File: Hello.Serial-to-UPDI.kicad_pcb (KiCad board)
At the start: 2 copper layers, 19.7 x 19 mm, 3 parts, among them J1 Conn_01x03_Male, J2 Conn_FTDI_01x06_Male

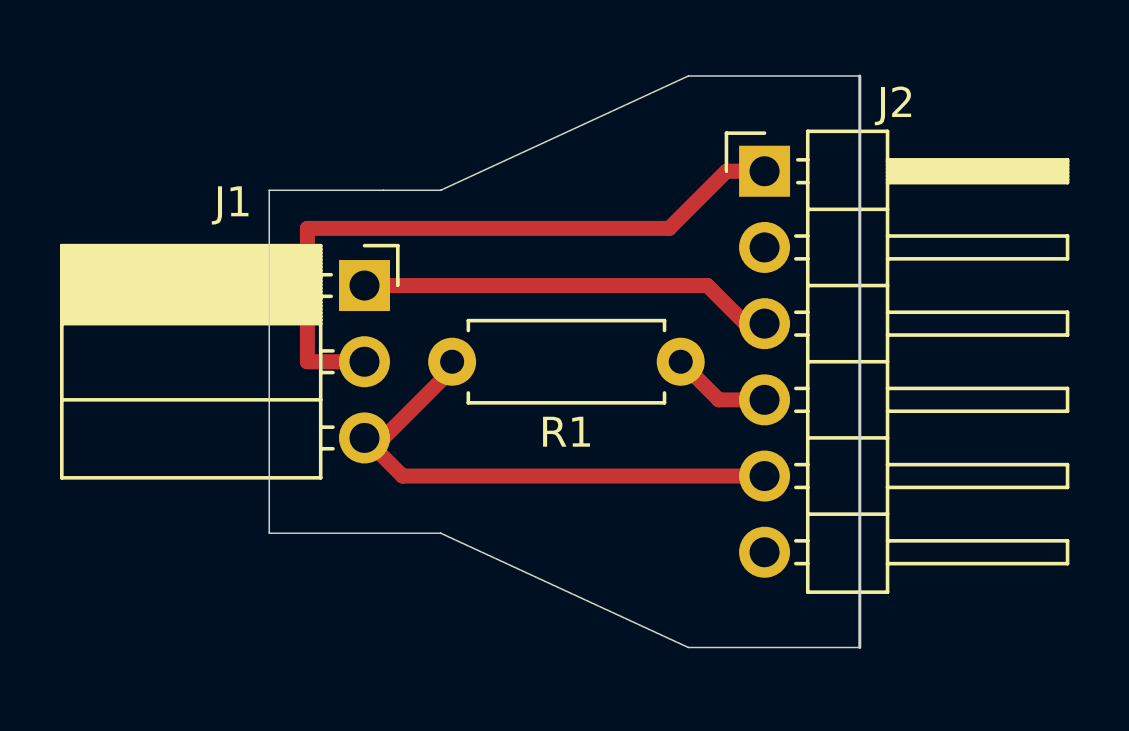
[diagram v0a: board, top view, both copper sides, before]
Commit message: Commit recent RML files, get rid of old SVGs
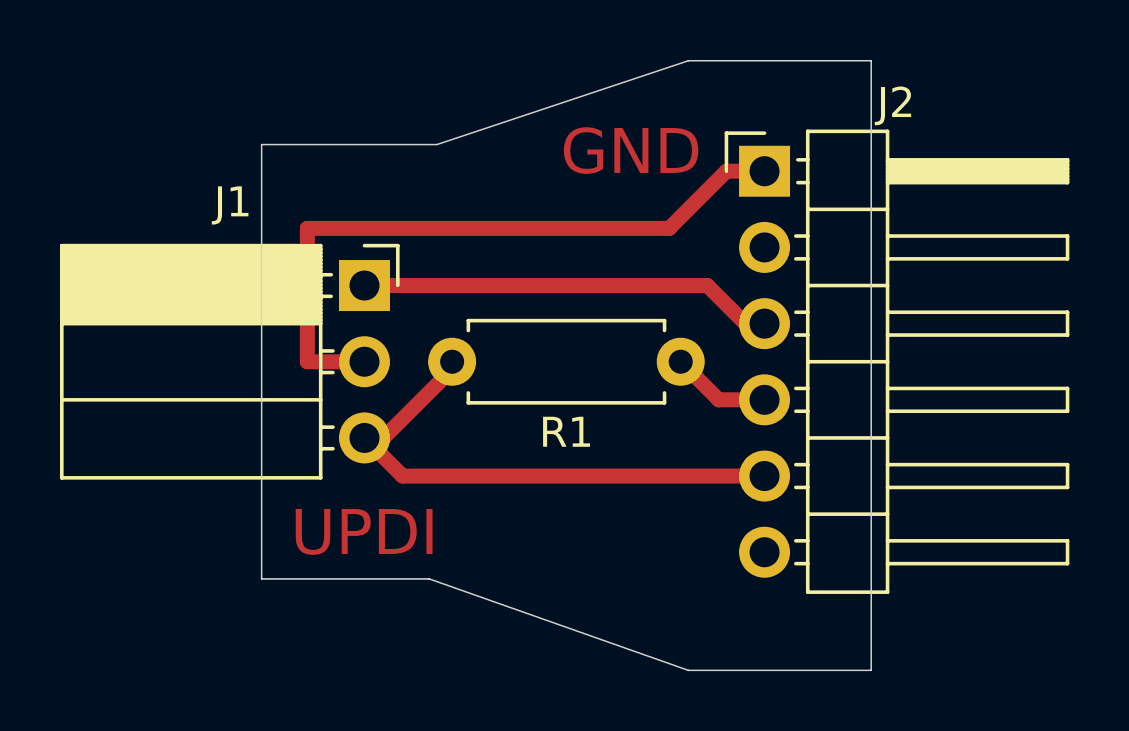
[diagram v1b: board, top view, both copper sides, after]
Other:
- board size 19.7 x 19 mm -> 20.3 x 20.3 mm
- board text added: "GND"
- board text added: "UPDI"
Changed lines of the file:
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@@
-(kicad_pcb (version 20171130) (host pcbnew "(5.1.9)-1")
+(kicad_pcb (version 20171130) (host pcbnew "(5.1.9-0-10_14)")
   (general
     (thickness 1.6)
@@
     (38 B.Mask user)
     (39 F.Mask user)
-    (40 Dwgs.User user hide)
+    (40 Dwgs.User user)
     (41 Cmts.User user)
     (42 Eco1.User user)
     (43 Eco2.User user)
     (44 Edge.Cuts user)
-    (45 Margin user hide)
+    (45 Margin user)
     (46 B.CrtYd user)
     (47 F.CrtYd user)
@@
   )
   (setup
-    (last_trace_width 0.5)
+    (last_trace_width 0.25)
     (user_trace_width 0.5)
     (trace_clearance 0.2)
@@
     (visible_elements 7FFFFFFF)
     (pcbplotparams
-      (layerselection 0x010fc_ffffffff)
+      (layerselection 0x00000_7fffffff)
       (usegerberextensions false)
       (usegerberattributes true)
@@
       (psnegative false)
       (psa4output false)
-      (plotreference true)
-      (plotvalue true)
+      (plotreference false)
+      (plotvalue false)
       (plotinvisibletext false)
-      (padsonsilk false)
+      (padsonsilk true)
       (subtractmaskfromsilk false)
-      (outputformat 1)
+      (outputformat 5)
       (mirror false)
-      (drillshape 1)
+      (drillshape 0)
       (scaleselection 1)
       (outputdirectory ""))
@@
       (effects (font (size 1 1) (thickness 0.15)))
     )
-    (fp_text user %R (at 3.81 0) (layer F.Fab)
-      (effects (font (size 1 1) (thickness 0.15)))
-    )
     (fp_line (start 0.66 -1.25) (end 0.66 1.25) (layer F.Fab) (width 0.1))
     (fp_line (start 0.66 1.25) (end 6.96 1.25) (layer F.Fab) (width 0.1))
@@
     (fp_line (start 8.67 1.5) (end 8.67 -1.5) (layer F.CrtYd) (width 0.05))
     (fp_line (start 8.67 -1.5) (end -1.05 -1.5) (layer F.CrtYd) (width 0.05))
+    (fp_text user %R (at 3.81 0) (layer F.Fab)
+      (effects (font (size 1 1) (thickness 0.15)))
+    )
     (pad 2 thru_hole oval (at 7.62 0 180) (size 1.6 1.6) (drill 0.8) (layers *.Cu *.Mask)
       (net 1 "Net-(J1-Pad3)"))
@@
     )
     (fp_text value Conn_FTDI_01x06_Male (at 4.385 14.97) (layer F.Fab)
-      (effects (font (size 1 1) (thickness 0.15)))
-    )
-    (fp_text user %R (at 2.77 6.35 90) (layer F.Fab)
       (effects (font (size 1 1) (thickness 0.15)))
     )
@@
     (fp_line (start 10.55 14.5) (end 10.55 -1.8) (layer F.CrtYd) (width 0.05))
     (fp_line (start 10.55 -1.8) (end -1.8 -1.8) (layer F.CrtYd) (width 0.05))
+    (fp_text user %R (at 2.77 6.35 90) (layer F.Fab)
+      (effects (font (size 1 1) (thickness 0.15)))
+    )
     (pad 6 thru_hole oval (at 0 12.7) (size 1.7 1.7) (drill 1) (layers *.Cu *.Mask)
       (net 4 "Net-(J2-Pad6)"))
@@
     )
   )
-  (module Connector_PinSocket_2.54mm:PinSocket_1x03_P2.54mm_Horizontal (layer F.Cu)
+  (module Connector_PinSocket_2.54mm:PinSocket_1x03_P2.54mm_Horizontal locked (layer F.Cu)
     (at 135.255 84.455)
     (descr "Through hole angled socket strip, 1x03, 2.54mm pitch, 8.51mm socket length, single row (from Kicad 4.0.7), script generated")
@@
     )
     (fp_text value Conn_01x03_Male (at -4.38 7.85) (layer F.Fab)
-      (effects (font (size 1 1) (thickness 0.15)))
-    )
-    (fp_text user %R (at -5.775 2.54) (layer F.Fab)
       (effects (font (size 1 1) (thickness 0.15)))
     )
@@
     (fp_line (start -10.55 6.85) (end 1.75 6.85) (layer F.CrtYd) (width 0.05))
     (fp_line (start 1.75 6.85) (end 1.75 -1.8) (layer F.CrtYd) (width 0.05))
+    (fp_text user %R (at -5.775 2.54) (layer F.Fab)
+      (effects (font (size 1 1) (thickness 0.15)))
+    )
     (pad 3 thru_hole oval (at 0 5.08) (size 1.7 1.7) (drill 1) (layers *.Cu *.Mask)
       (net 1 "Net-(J1-Pad3)"))
@@
     )
   )
-  (gr_poly (pts (xy 151.765 96.52) (xy 146.05 96.52) (xy 137.795 92.71) (xy 132.08 92.71) (xy 132.08 81.28) (xy 137.795 81.28) (xy 146.05 77.47) (xy 151.765 77.47)) (layer Dwgs.User) (width 0.1))
-  (gr_line (start 132.08 81.28) (end 132.08 92.71) (layer Edge.Cuts) (width 0.05))
-  (gr_line (start 151.765 77.47) (end 151.765 96.52) (layer Edge.Cuts) (width 0.1))
-  (gr_line (start 146.05 96.52) (end 151.765 96.52) (layer Edge.Cuts) (width 0.05))
-  (gr_line (start 137.795 92.71) (end 146.05 96.52) (layer Edge.Cuts) (width 0.05))
-  (gr_line (start 132.08 92.71) (end 137.795 92.71) (layer Edge.Cuts) (width 0.05))
-  (gr_line (start 137.795 81.28) (end 135.89 81.28) (layer Edge.Cuts) (width 0.05))
-  (gr_line (start 146.05 77.47) (end 137.795 81.28) (layer Edge.Cuts) (width 0.05))
-  (gr_line (start 151.765 77.47) (end 146.05 77.47) (layer Edge.Cuts) (width 0.05))
-  (gr_line (start 132.08 81.28) (end 135.89 81.28) (layer Edge.Cuts) (width 0.05))
-  (gr_poly (pts (xy 152.4 97.79) (xy 131.445 97.79) (xy 131.445 76.835) (xy 152.4 76.835)) (layer Margin) (width 0.1))
+  (gr_line (start 131.826 79.756) (end 131.826 94.234) (layer Edge.Cuts) (width 0.05))
+  (gr_line (start 137.668 79.756) (end 131.826 79.756) (layer Edge.Cuts) (width 0.05))
+  (gr_line (start 146.05 76.962) (end 137.668 79.756) (layer Edge.Cuts) (width 0.05))
+  (gr_line (start 152.146 76.962) (end 146.05 76.962) (layer Edge.Cuts) (width 0.05))
+  (gr_line (start 152.146 97.282) (end 152.146 76.962) (layer Edge.Cuts) (width 0.05))
+  (gr_line (start 146.05 97.282) (end 152.146 97.282) (layer Edge.Cuts) (width 0.05))
+  (gr_line (start 137.414 94.234) (end 146.05 97.282) (layer Edge.Cuts) (width 0.05))
+  (gr_line (start 131.826 94.234) (end 137.414 94.234) (layer Edge.Cuts) (width 0.05))
+  (gr_text GND (at 144.145 80.01) (layer F.Cu)
+    (effects (font (size 1.5 1.5) (thickness 0.3)))
+  )
+  (gr_text UPDI (at 135.255 92.71) (layer F.Cu)
+    (effects (font (size 1.5 1.5) (thickness 0.3)))
+  )
+  (gr_poly (pts (xy 151.765 96.52) (xy 146.05 96.52) (xy 137.4775 93.98) (xy 132.08 93.98) (xy 132.08 80.01) (xy 137.795 80.01) (xy 146.05 77.47) (xy 151.765 77.47)) (layer Dwgs.User) (width 0.1))
   (segment (start 135.255 89.535) (end 136.525 90.805) (width 0.5) (layer F.Cu) (net 1))
   (segment (start 136.525 90.805) (end 148.59 90.805) (width 0.5) (layer F.Cu) (net 1))
-  (segment (start 135.255 89.535) (end 135.89 89.535) (width 0.5) (layer F.Cu) (net 1))
   (segment (start 138.176 87.249) (end 138.176 86.995) (width 0.5) (layer F.Cu) (net 1))
   (segment (start 135.89 89.535) (end 138.176 87.249) (width 0.5) (layer F.Cu) (net 1))
+  (segment (start 135.255 89.535) (end 135.89 89.535) (width 0.5) (layer F.Cu) (net 1))
+  (segment (start 135.255 86.995) (end 133.35 86.995) (width 0.5) (layer F.Cu) (net 2))
+  (segment (start 133.35 86.995) (end 133.35 82.55) (width 0.5) (layer F.Cu) (net 2))
+  (segment (start 133.35 82.55) (end 145.415 82.55) (width 0.5) (layer F.Cu) (net 2))
+  (segment (start 145.415 82.55) (end 147.32 80.645) (width 0.5) (layer F.Cu) (net 2))
   (segment (start 147.32 80.645) (end 148.59 80.645) (width 0.5) (layer F.Cu) (net 2))
-  (segment (start 145.415 82.55) (end 147.32 80.645) (width 0.5) (layer F.Cu) (net 2))
-  (segment (start 133.35 82.55) (end 145.415 82.55) (width 0.5) (layer F.Cu) (net 2))
-  (segment (start 133.35 86.995) (end 133.35 82.55) (width 0.5) (layer F.Cu) (net 2))
-  (segment (start 135.255 86.995) (end 133.35 86.995) (width 0.5) (layer F.Cu) (net 2))
+  (segment (start 135.255 84.455) (end 146.685 84.455) (width 0.5) (layer F.Cu) (net 3))
+  (segment (start 146.685 84.455) (end 147.955 85.725) (width 0.5) (layer F.Cu) (net 3))
   (segment (start 147.955 85.725) (end 148.59 85.725) (width 0.5) (layer F.Cu) (net 3))
-  (segment (start 146.685 84.455) (end 147.955 85.725) (width 0.5) (layer F.Cu) (net 3))
-  (segment (start 135.255 84.455) (end 146.685 84.455) (width 0.5) (layer F.Cu) (net 3))
+  (segment (start 147.066 88.265) (end 148.59 88.265) (width 0.5) (layer F.Cu) (net 5))
   (segment (start 145.796 86.995) (end 147.066 88.265) (width 0.5) (layer F.Cu) (net 5))
-  (segment (start 147.066 88.265) (end 148.59 88.265) (width 0.5) (layer F.Cu) (net 5))
 )
